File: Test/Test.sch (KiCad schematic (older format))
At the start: 6 parts, among them Q1 ZVN3306F

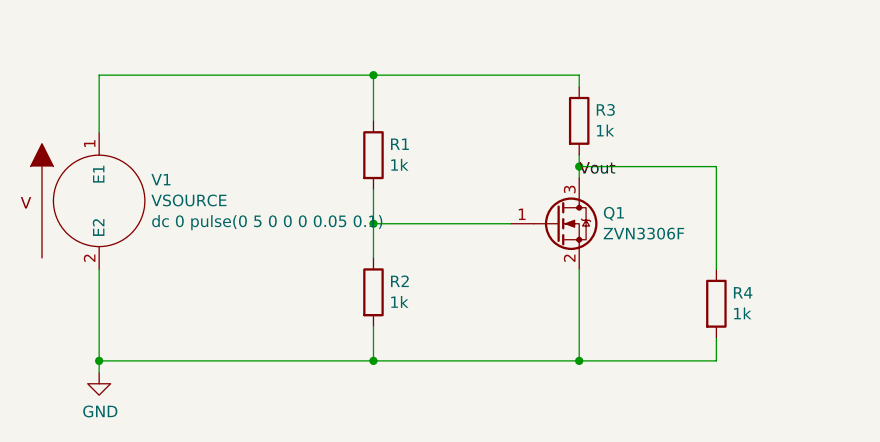
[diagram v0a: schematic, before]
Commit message: Added Multisim File for testing Fan Circuitry and MOSFET spice models
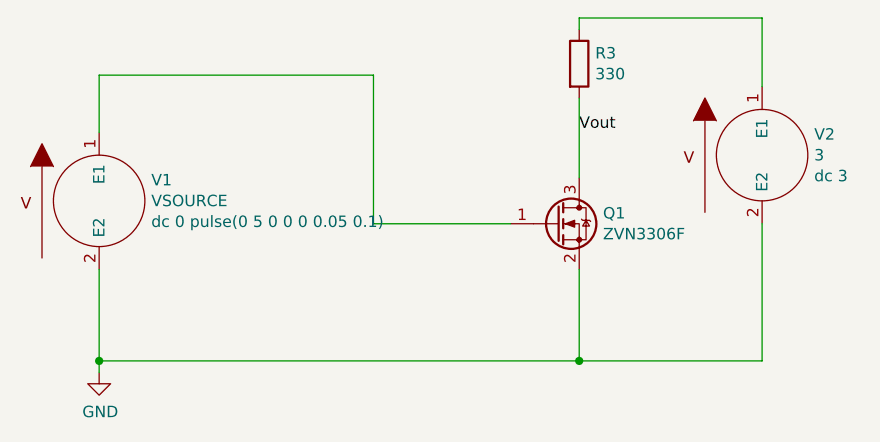
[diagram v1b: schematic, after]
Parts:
- removed R1, R2, R4: 1k, symbol Device:R
- added V2: 3, symbol pspice:VSOURCE
- Q1: Spice_Lib_File (none) -> C:\\Users\\Nripesh\\Documents\\UVA\\Solar Car\\PowerTeam\\Z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; Spice_Model (none) -> ZVN3306F; Spice_Netlist_Enabled (none) -> Y; Spice_Primitive (none) -> X
- R3: value 1k -> 330
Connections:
- net GND: now also V2.2 (E2)
- net at V1.1 (E1): now also Q1.1 (G); no longer R3.1
- new net: R3.1, V2.1 (E1)
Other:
- moved on the sheet: R3
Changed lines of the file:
@@
 $EndDescr
+$Comp
+L power:GND #PWR01
+U 1 1 5E9A5E60
+P 1000 2650
+F 0 "#PWR01" H 1000 2400 50  0001 C CNN
+F 1 "GND" H 1005 2477 50  0000 C CNN
+F 2 "" H 1000 2650 50  0001 C CNN
+F 3 "" H 1000 2650 50  0001 C CNN
+	1    1000 2650
+	1    0    0    -1
+$EndComp
+Wire Wire Line
+	1000 1600 1000 1350
+Wire Wire Line
+	1000 2600 1000 2200
+Wire Wire Line
+	1000 2650 1000 2600
+Connection ~ 1000 2600
+Wire Wire Line
+	2200 2000 2800 2000
+$Comp
+L Device:R R3
+U 1 1 5E9B1BD5
+P 3100 1300
+F 0 "R3" H 3170 1346 50  0000 L CNN
+F 1 "330" H 3170 1255 50  0000 L CNN
+F 2 "" V 3030 1300 50  0001 C CNN
+F 3 "~" H 3100 1300 50  0001 C CNN
+	1    3100 1300
+	1    0    0    -1
+$EndComp
+Wire Wire Line
+	3100 1100 3100 1150
+Text Label 3100 1600 0    50   ~ 0
+Vout
+Wire Wire Line
+	1000 1350 2200 1350
 $Comp
 L pspice:VSOURCE V1
@@
 	1    0    0    -1
 $EndComp
+Wire Wire Line
+	3900 2600 3100 2600
+Connection ~ 3100 2600
+Wire Wire Line
+	3100 2200 3100 2600
+Wire Wire Line
+	3100 1100 3900 1100
+Wire Wire Line
+	1000 2600 3100 2600
+Wire Wire Line
+	2200 1350 2200 2000
 $Comp
-L power:GND #PWR01
-U 1 1 5E9A5E60
-P 1000 2650
-F 0 "#PWR01" H 1000 2400 50  0001 C CNN
-F 1 "GND" H 1005 2477 50  0000 C CNN
-F 2 "" H 1000 2650 50  0001 C CNN
-F 3 "" H 1000 2650 50  0001 C CNN
-	1    1000 2650
-	1    0    0    -1
-$EndComp
-$Comp
-L Device:R R1
-U 1 1 5E9A62A9
-P 2200 1700
-F 0 "R1" H 2270 1746 50  0000 L CNN
-F 1 "1k" H 2270 1655 50  0000 L CNN
-F 2 "" V 2130 1700 50  0001 C CNN
-F 3 "~" H 2200 1700 50  0001 C CNN
-	1    2200 1700
-	1    0    0    -1
-$EndComp
-$Comp
-L Device:R R2
-U 1 1 5E9A67DE
-P 2200 2300
-F 0 "R2" H 2270 2346 50  0000 L CNN
-F 1 "1k" H 2270 2255 50  0000 L CNN
-F 2 "" V 2130 2300 50  0001 C CNN
-F 3 "~" H 2200 2300 50  0001 C CNN
-	1    2200 2300
+L pspice:VSOURCE V2
+U 1 1 5E9E5CD9
+P 3900 1700
+F 0 "V2" H 4128 1791 50  0000 L CNN
+F 1 "3" H 4128 1700 50  0000 L CNN
+F 2 "" H 3900 1700 50  0001 C CNN
+F 3 "~" H 3900 1700 50  0001 C CNN
+F 4 "V" H 3900 1700 50  0001 C CNN "Spice_Primitive"
+F 5 "dc 3" H 4128 1609 50  0000 L CNN "Spice_Model"
+F 6 "Y" H 3900 1700 50  0001 C CNN "Spice_Netlist_Enabled"
+	1    3900 1700
 	1    0    0    -1
 $EndComp
 Wire Wire Line
-	1000 1600 1000 1350
+	3900 2000 3900 2600
 Wire Wire Line
-	1000 1350 2200 1350
+	3100 1450 3100 1800
 Wire Wire Line
-	2200 1350 2200 1550
-Wire Wire Line
-	2200 2600 1000 2600
-Wire Wire Line
-	1000 2600 1000 2200
-Wire Wire Line
-	2200 1850 2200 2000
-Wire Wire Line
-	2200 2450 2200 2600
-Wire Wire Line
-	1000 2650 1000 2600
-Connection ~ 1000 2600
+	3900 1100 3900 1400
 $Comp
 L Transistor_FET:ZVN3306F Q1
-U 1 1 5E9A7EC6
+U 1 1 5E9EA4AB
 P 3000 2000
 F 0 "Q1" H 3204 2046 50  0000 L CNN
@@
 F 2 "Package_TO_SOT_SMD:SOT-23" H 3200 1925 50  0001 L CIN
 F 3 "http://www.diodes.com/assets/Datasheets/ZVN3306F.pdf" H 3000 2000 50  0001 L CNN
+F 4 "X" H 3000 2000 50  0001 C CNN "Spice_Primitive"
+F 5 "ZVN3306F" H 3000 2000 50  0001 C CNN "Spice_Model"
+F 6 "Y" H 3000 2000 50  0001 C CNN "Spice_Netlist_Enabled"
+F 7 "C:\\Users\\Nripesh\\Documents\\UVA\\Solar Car\\PowerTeam\\ZVN3306F.spice.txt" H 3000 2000 50  0001 C CNN "Spice_Lib_File"
 	1    3000 2000
 	1    0    0    -1
 $EndComp
-Wire Wire Line
-	2200 2000 2800 2000
-Connection ~ 2200 2000
-Wire Wire Line
-	2200 2000 2200 2150
-Wire Wire Line
-	3100 2200 3100 2600
-Wire Wire Line
-	3100 2600 2200 2600
-Connection ~ 2200 2600
-$Comp
-L Device:R R3
-U 1 1 5E9B1BD5
-P 3100 1550
-F 0 "R3" H 3170 1596 50  0000 L CNN
-F 1 "1k" H 3170 1505 50  0000 L CNN
-F 2 "" V 3030 1550 50  0001 C CNN
-F 3 "~" H 3100 1550 50  0001 C CNN
-	1    3100 1550
-	1    0    0    -1
-$EndComp
-Wire Wire Line
-	2200 1350 3100 1350
-Wire Wire Line
-	3100 1350 3100 1400
-Wire Wire Line
-	3100 1700 3100 1750
-Connection ~ 2200 1350
-Text Label 3100 1800 0    50   ~ 0
-Vout
-Wire Wire Line
-	3100 1750 3700 1750
-Wire Wire Line
-	3700 2600 3100 2600
-Connection ~ 3100 1750
-Wire Wire Line
-	3100 1750 3100 1800
-Connection ~ 3100 2600
-$Comp
-L Device:R R4
-U 1 1 5E98BBEA
-P 3700 2350
-F 0 "R4" H 3770 2396 50  0000 L CNN
-F 1 "1k" H 3770 2305 50  0000 L CNN
-F 2 "" V 3630 2350 50  0001 C CNN
-F 3 "~" H 3700 2350 50  0001 C CNN
-	1    3700 2350
-	1    0    0    -1
-$EndComp
-Wire Wire Line
-	3700 2500 3700 2600
-Wire Wire Line
-	3700 1750 3700 2200
 $EndSCHEMATC
